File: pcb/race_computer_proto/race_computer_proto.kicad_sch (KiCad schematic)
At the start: 12 parts, among them U1 Teensy4.0, U3 SN74LVC245APW

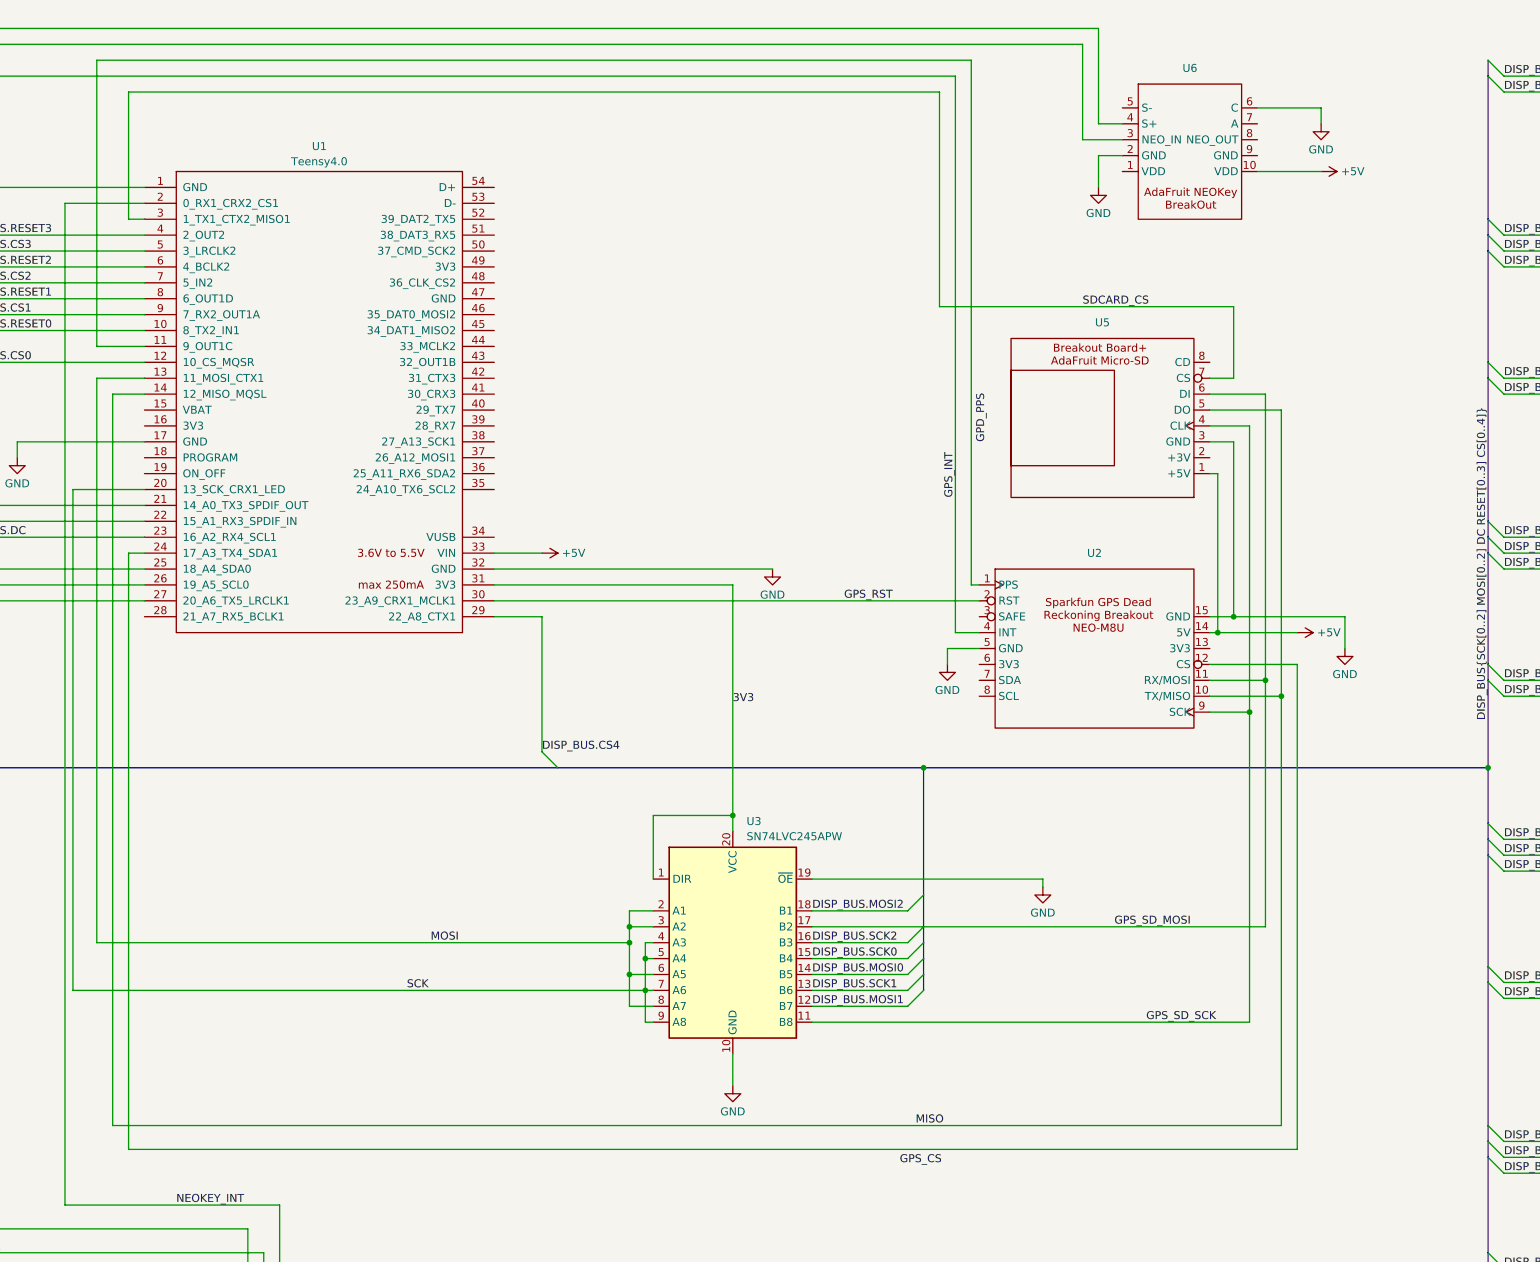
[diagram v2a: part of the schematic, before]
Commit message: PCB redesign.  OLEDs and other secondary modules moved off board and replaced with headers for cable connections. Only Teensy and GPS modules remain on primary board.
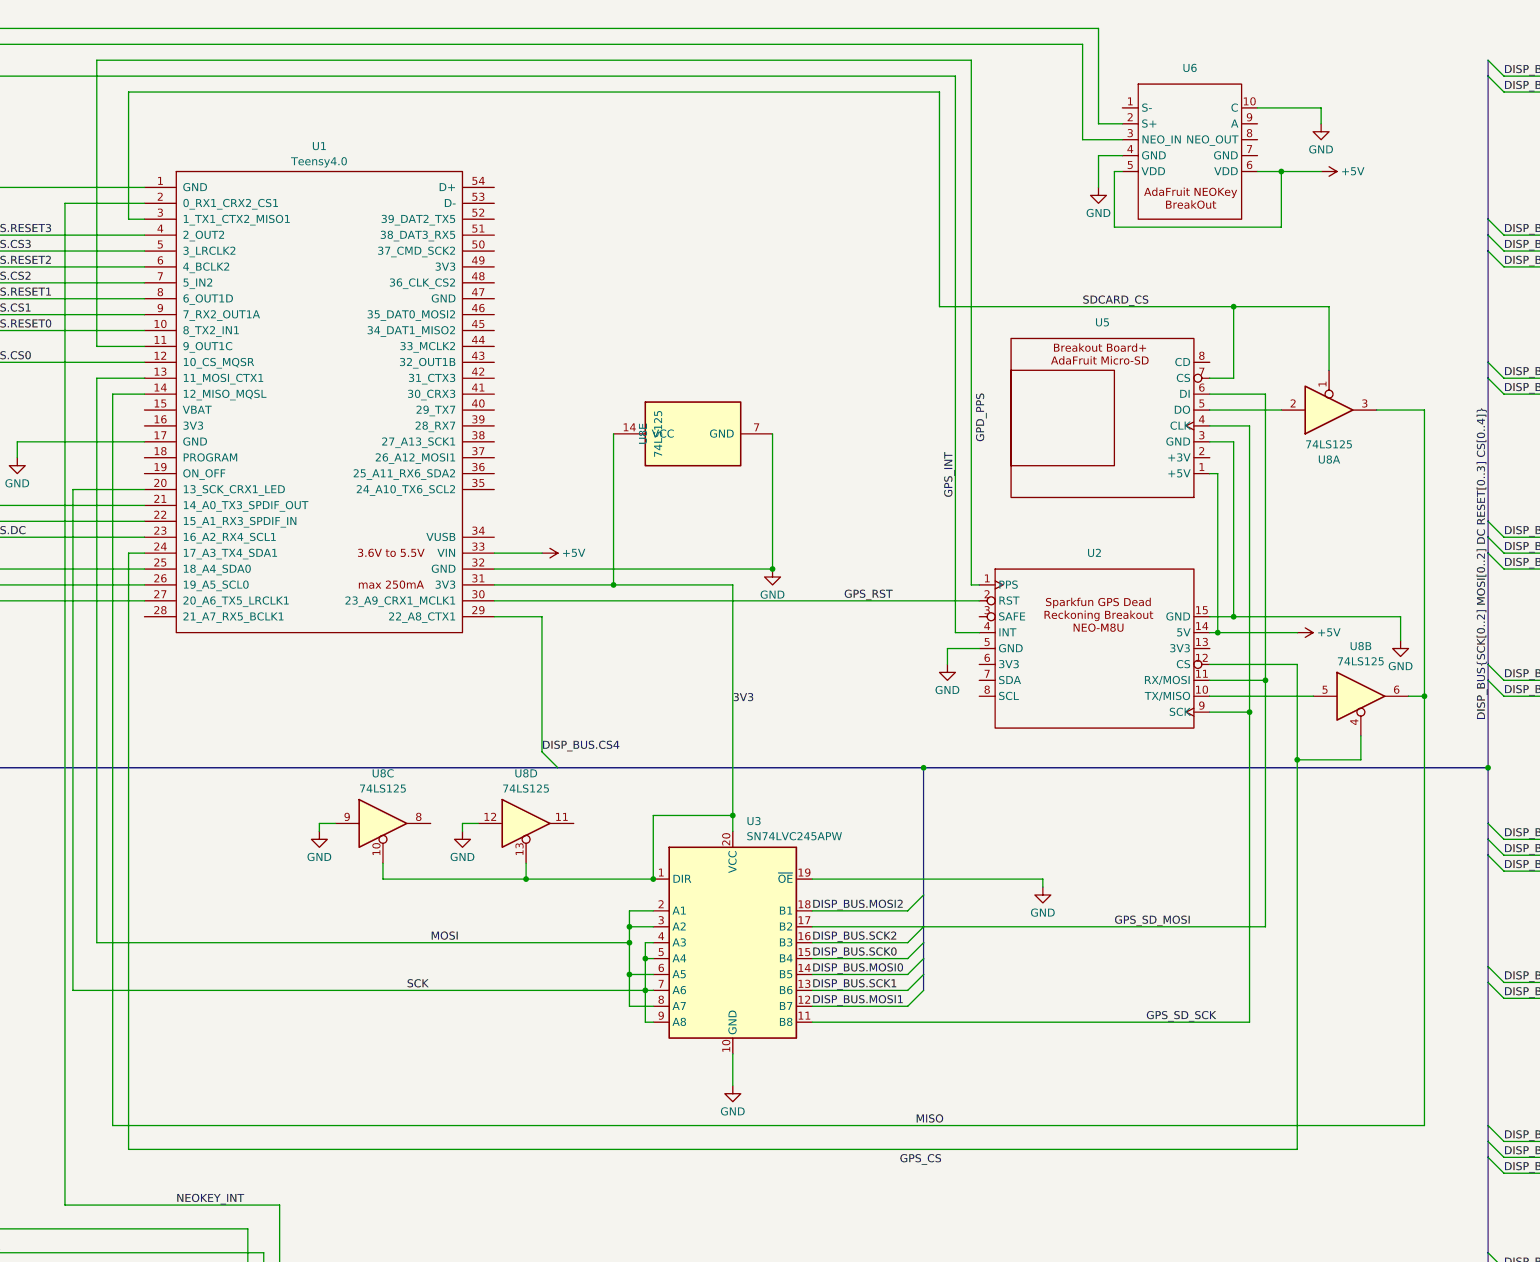
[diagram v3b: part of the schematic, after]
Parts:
- added U8: 74LS125, Package_DIP:DIP-14_W7.62mm_Socket_LongPads, symbol 74xx:74LS125
- LED1: footprint race_computer:8-Digit 7 Segment MAX7219 Module -> race_computer:7seg_max7219_module_header
- OD1, OD2, OD3, OD4: footprint race_computer:OLED_Display -> race_computer:OLED_header
- U4: footprint race_computer:AdaFruit_USB_C_PD -> race_computer:power_header
- U5: footprint race_computer:AdaFruit_MicroSD+ -> race_computer:microsd_breakout_header
- U6: footprint race_computer:neokey_MX_breakout -> race_computer:neokey_header
- U7: footprint race_computer:NeoKey1x4 -> race_computer:neokey_1x4_header
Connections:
- net +5V: now also U6.5 (VDD), U6.6 (VDD); no longer U6.10 (VDD)
- net 3V3: now also U8.10, U8.13, U8.14 (VCC)
- net GND: now also U6.10 (C), U6.4 (GND), U8.12, U8.7 (GND), U8.9; no longer U6.2 (GND), U6.6 (C)
- net MISO: now also U8.3, U8.6; no longer U2.10 (TX/MISO), U5.5 (DO)
- net SDCARD_CS: now also U8.1
- net at U1.22 (15_A1_RX3_SPDIF_IN): now also U6.2 (S+); no longer U6.4 (S+)
- net at U1.24 (17_A3_TX4_SDA1), U2.12 (CS): now also U8.4
- new net: U5.5 (DO), U8.2
- new net: U2.10 (TX/MISO), U8.5

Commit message: Add rev info to schematic sheet.  Remove gerbers and other unneeded files from repo.
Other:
- title: (none) -> Open Race Computer
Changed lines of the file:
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@@
 	(generator_version "8.0")
 	(paper "A3")
+	(title_block
+		(title "Open Race Computer")
+		(date "2025-12-20")
+		(rev "1.1")
+	)
 	(junction
 		(at 166.37 143.51)

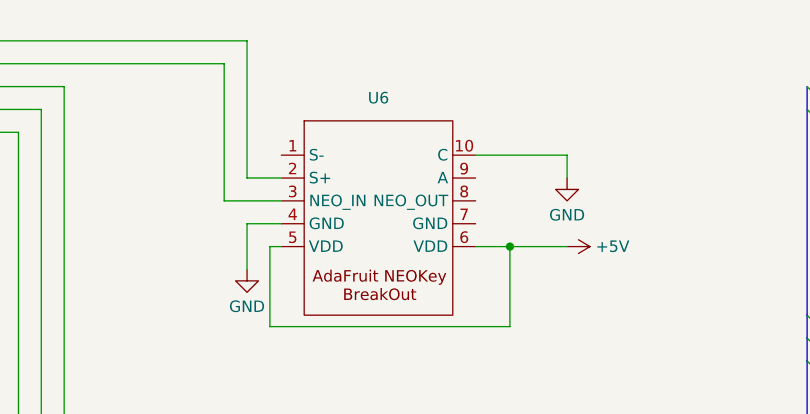
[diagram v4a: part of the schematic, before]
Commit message: Updated case for the new PCB.  Includes models for electronics. Minor PCB fix -- GND connection was missing from the NeoKey connector, so the button would not register when pushed.
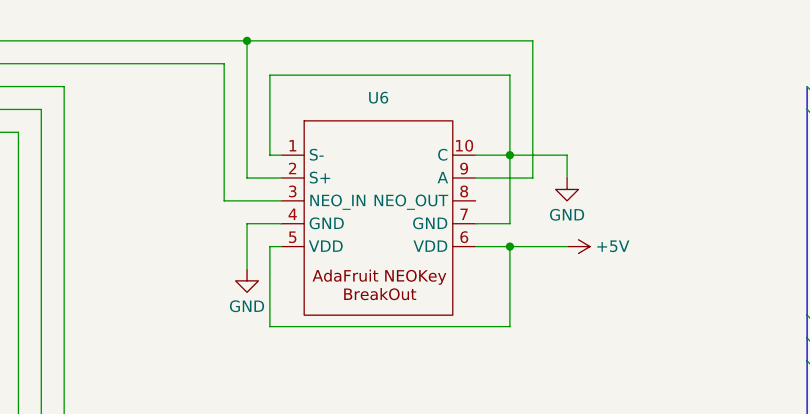
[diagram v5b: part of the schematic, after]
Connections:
- net GND: now also U6.1 (S-), U6.7 (GND)
- net at U1.22 (15_A1_RX3_SPDIF_IN), U6.2 (S+): now also U6.9 (A)
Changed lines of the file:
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@@
+	)
+	(junction
+		(at 224.79 17.78)
+		(diameter 0)
+		(color 0 0 0 0)
 	)
 	(junction
@@
 	(junction
 		(at 152.4 171.45)
+		(diameter 0)
+		(color 0 0 0 0)
+	)
+	(junction
+		(at 254 30.48)
 		(diameter 0)
 		(color 0 0 0 0)
@@
 	(wire
 		(pts
+			(xy 254 38.1) (xy 254 30.48)
+		)
+		(stroke
+			(width 0)
+			(type default)
+		)
+	)
+	(wire
+		(pts
 			(xy 308.61 213.36) (xy 309.88 213.36)
 		)
@@
 	(wire
 		(pts
+			(xy 227.33 21.59) (xy 254 21.59)
+		)
+		(stroke
+			(width 0)
+			(type default)
+		)
+	)
+	(wire
+		(pts
 			(xy 128.27 106.68) (xy 147.32 106.68)
 		)
@@
 	(wire
 		(pts
+			(xy 254 21.59) (xy 254 30.48)
+		)
+		(stroke
+			(width 0)
+			(type default)
+		)
+	)
+	(wire
+		(pts
 			(xy 227.33 49.53) (xy 254 49.53)
 		)
@@
 		)
 	)
+	(wire
+		(pts
+			(xy 224.79 17.78) (xy 256.54 17.78)
+		)
+		(stroke
+			(width 0)
+			(type default)
+		)
+	)
 	(bus
 		(pts
@@
 		)
 	)
+	(wire
+		(pts
+			(xy 254 30.48) (xy 260.35 30.48)
+		)
+		(stroke
+			(width 0)
+			(type default)
+		)
+	)
 	(bus
 		(pts
@@
 	(wire
 		(pts
+			(xy 227.33 30.48) (xy 227.33 21.59)
+		)
+		(stroke
+			(width 0)
+			(type default)
+		)
+	)
+	(wire
+		(pts
 			(xy 309.88 66.04) (xy 308.61 66.04)
 		)
@@
 	(wire
 		(pts
+			(xy 250.19 38.1) (xy 254 38.1)
+		)
+		(stroke
+			(width 0)
+			(type default)
+		)
+	)
+	(wire
+		(pts
 			(xy 307.34 165.1) (xy 307.34 116.84)
 		)
@@
 	(wire
 		(pts
-			(xy 250.19 30.48) (xy 260.35 30.48)
+			(xy 250.19 30.48) (xy 254 30.48)
 		)
 		(stroke
@@
 	(wire
 		(pts
+			(xy 250.19 33.02) (xy 256.54 33.02)
+		)
+		(stroke
+			(width 0)
+			(type default)
+		)
+	)
+	(wire
+		(pts
 			(xy 307.34 210.82) (xy 307.34 165.1)
 		)
@@
 	(wire
 		(pts
+			(xy 228.6 30.48) (xy 227.33 30.48)
+		)
+		(stroke
+			(width 0)
+			(type default)
+		)
+	)
+	(wire
+		(pts
 			(xy 307.34 224.79) (xy 307.34 210.82)
 		)
@@
 		)
 		(stroke
+			(width 0)
+			(type default)
+		)
+	)
+	(wire
+		(pts
+			(xy 256.54 33.02) (xy 256.54 17.78)
+		)
+		(stroke
